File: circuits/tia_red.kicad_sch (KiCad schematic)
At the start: 11 parts, among them U2 OPA380AID

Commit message: Checkpoint laser controller fab parity package
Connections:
- net PD_CATHODE: now reaches C7.1, D2.1 (K), R6.2
- net PD_ANODE: now reaches C5.1, D2.2 (A), RV6.1, U2.2 (-)
- net VBIAS: now reaches C8.1, R7.2, U2.3 (+)
- net VBIAS_TOP: now reaches R8.2, RV2.1
- net VBIAS_WIPER: now reaches R7.1, RV2.2 (W)
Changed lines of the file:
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@@
   (no_connect (at 224.79 154.94))
   (no_connect (at 224.79 144.78))
+  (label "PD_ANODE" (at 190.5 130.81 0) (effects (font (size 1.27 1.27)) (justify left bottom)))
+  (label "PD_CATHODE" (at 185.42 130.81 0) (effects (font (size 1.27 1.27)) (justify left bottom)))
+  (label "VBIAS_TOP" (at 165.1 143.51 0) (effects (font (size 1.27 1.27)) (justify left bottom)))
+  (label "VBIAS_WIPER" (at 168.91 152.4 0) (effects (font (size 1.27 1.27)) (justify left bottom)))
+  (label "VBIAS" (at 190.5 152.4 0) (effects (font (size 1.27 1.27)) (justify left bottom)))
   (hierarchical_label "V_OUT" (shape output) (at 232.41 149.86 0) (effects (font (size 1.27 1.27)) (justify left)))
   (text "TIA Channel  —  on-board SFH2201 signal PD → OPA380AID transimpedance amp  ·  reused 4× (IR / RED / GREEN / BLUE)" (at 150 104 0) (effects (font (size 2.0 2.0)) (justify left)))

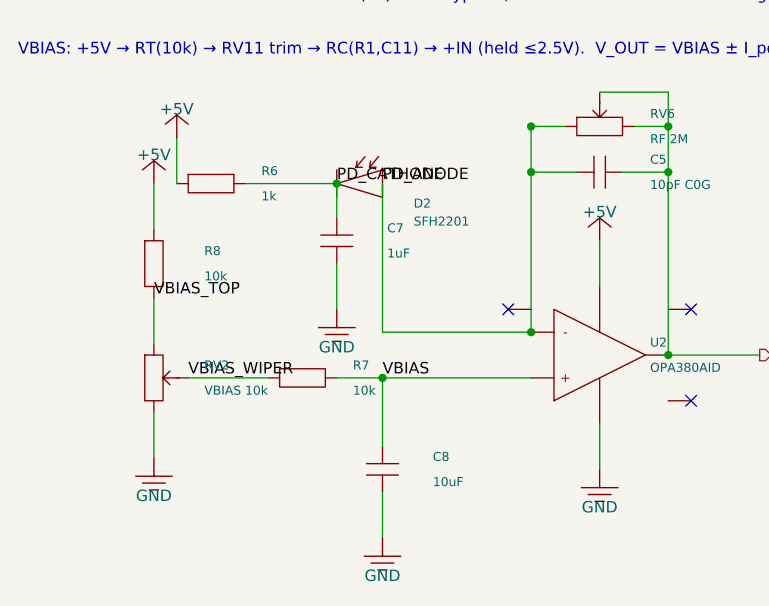
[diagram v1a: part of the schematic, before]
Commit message: Checkpoint schematic warning hygiene
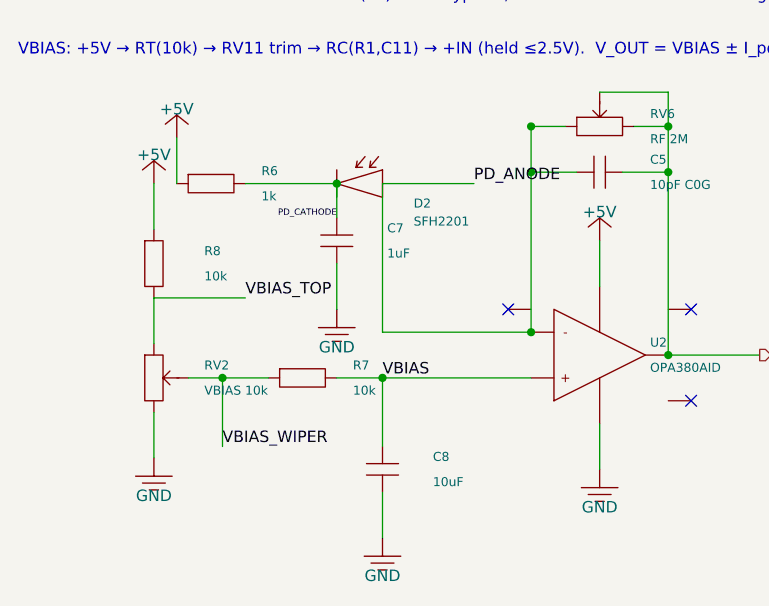
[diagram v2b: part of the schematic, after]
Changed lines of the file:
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@@
   (wire (pts (xy 167.64 130.81) (xy 167.64 125.73)) (stroke (width 0) (type default)))
   (wire (pts (xy 185.42 139.7) (xy 185.42 144.78)) (stroke (width 0) (type default)))
+  (wire (pts (xy 190.5 130.81) (xy 200.66 130.81)) (stroke (width 0) (type default)))
   (wire (pts (xy 207.01 147.32) (xy 207.01 129.54)) (stroke (width 0) (type default)))
   (wire (pts (xy 207.01 129.54) (xy 207.01 124.46)) (stroke (width 0) (type default)))
@@
   (wire (pts (xy 190.5 165.1) (xy 190.5 170.18)) (stroke (width 0) (type default)))
   (wire (pts (xy 165.1 143.51) (xy 165.1 148.59)) (stroke (width 0) (type default)))
-  (wire (pts (xy 168.91 152.4) (xy 177.8 152.4)) (stroke (width 0) (type default)))
+  (wire (pts (xy 168.91 152.4) (xy 172.72 152.4)) (stroke (width 0) (type default)))
+  (wire (pts (xy 172.72 152.4) (xy 177.8 152.4)) (stroke (width 0) (type default)))
   (wire (pts (xy 185.42 152.4) (xy 190.5 152.4)) (stroke (width 0) (type default)))
   (wire (pts (xy 190.5 152.4) (xy 190.5 160.02)) (stroke (width 0) (type default)))
   (wire (pts (xy 190.5 152.4) (xy 207.01 152.4)) (stroke (width 0) (type default)))
+  (wire (pts (xy 165.1 143.51) (xy 175.26 143.51)) (stroke (width 0) (type default)))
+  (wire (pts (xy 172.72 152.4) (xy 172.72 160.02)) (stroke (width 0) (type default)))
   (junction (at 207.01 147.32) (diameter 0) (color 0 0 0 0))
   (junction (at 185.42 130.81) (diameter 0) (color 0 0 0 0))
@@
   (junction (at 222.25 149.86) (diameter 0) (color 0 0 0 0))
   (junction (at 190.5 152.4) (diameter 0) (color 0 0 0 0))
+  (junction (at 172.72 152.4) (diameter 0) (color 0 0 0 0))
   (no_connect (at 204.47 144.78))
   (no_connect (at 224.79 154.94))
   (no_connect (at 224.79 144.78))
-  (label "PD_ANODE" (at 190.5 130.81 0) (effects (font (size 1.27 1.27)) (justify left bottom)))
-  (label "PD_CATHODE" (at 185.42 130.81 0) (effects (font (size 1.27 1.27)) (justify left bottom)))
-  (label "VBIAS_TOP" (at 165.1 143.51 0) (effects (font (size 1.27 1.27)) (justify left bottom)))
-  (label "VBIAS_WIPER" (at 168.91 152.4 0) (effects (font (size 1.27 1.27)) (justify left bottom)))
+  (label "PD_ANODE" (at 200.66 130.81 0) (effects (font (size 1.27 1.27)) (justify left bottom)))
+  (label "PD_CATHODE" (at 185.42 134.62 0) (effects (font (size 0.7 0.7)) (justify right bottom)))
+  (label "VBIAS_TOP" (at 175.26 143.51 0) (effects (font (size 1.27 1.27)) (justify left bottom)))
+  (label "VBIAS_WIPER" (at 172.72 160.02 0) (effects (font (size 1.27 1.27)) (justify left bottom)))
   (label "VBIAS" (at 190.5 152.4 0) (effects (font (size 1.27 1.27)) (justify left bottom)))
   (hierarchical_label "V_OUT" (shape output) (at 232.41 149.86 0) (effects (font (size 1.27 1.27)) (justify left)))
